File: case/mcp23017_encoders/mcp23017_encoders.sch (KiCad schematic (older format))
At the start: 7 parts

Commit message: revised schematic for pin numbering
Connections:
- net WiringPi_26 renamed WiringPi_27
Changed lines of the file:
@@
 $EndComp
 Text GLabel 6100 2700 2    60   Input ~ 0
-WiringPi_26
+WiringPi_27
 Text GLabel 6100 2600 2    60   Input ~ 0
 WiringPi_25

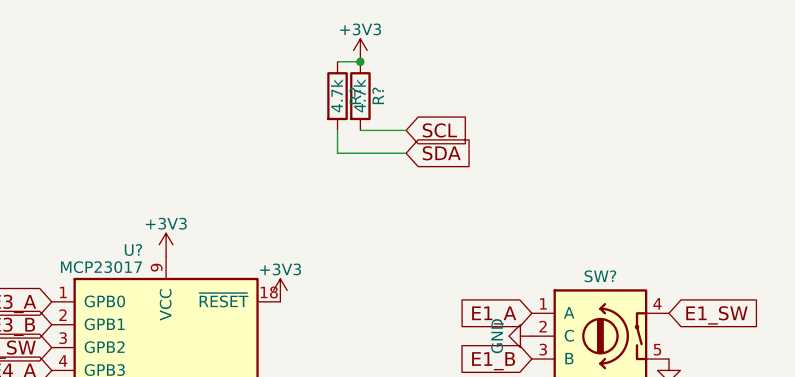
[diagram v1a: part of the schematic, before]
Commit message: removed pullups tt are not necessary on the raspberry pi
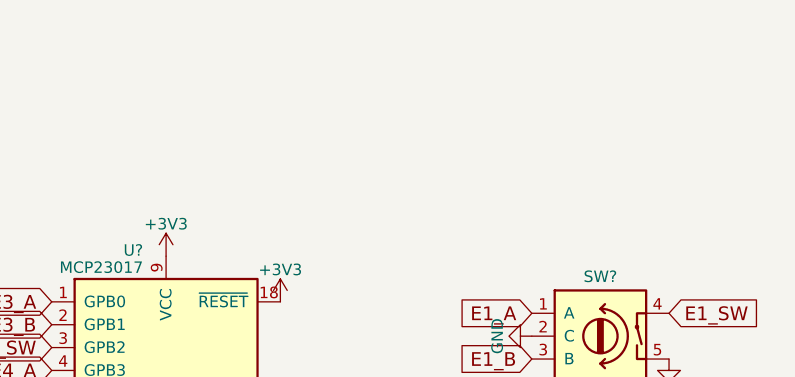
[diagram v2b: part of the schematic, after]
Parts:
- removed R? (x2): 4.7k, symbol R
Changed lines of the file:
@@
 	1    0    0    -1
 $EndComp
-Text GLabel 6650 1450 2    60   Input ~ 0
-SCL
-Text GLabel 6650 1550 2    60   Input ~ 0
-SDA
 Text GLabel 6100 3400 2    60   Input ~ 0
 SDA
 Text GLabel 6100 3300 2    60   Input ~ 0
 SCL
-$Comp
-L +3V3 #PWR?
-U 1 1 5936D9C5
-P 6450 1150
-F 0 "#PWR?" H 6450 1000 50  0001 C CNN
-F 1 "+3V3" H 6450 1290 50  0000 C CNN
-F 2 "" H 6450 1150 50  0001 C CNN
-F 3 "" H 6450 1150 50  0001 C CNN
-	1    6450 1150
-	1    0    0    -1
-$EndComp
-$Comp
-L R R?
-U 1 1 5936D9DF
-P 6450 1300
-F 0 "R?" V 6530 1300 50  0000 C CNN
-F 1 "4.7k" V 6450 1300 50  0000 C CNN
-F 2 "" V 6380 1300 50  0001 C CNN
-F 3 "" H 6450 1300 50  0001 C CNN
-	1    6450 1300
-	1    0    0    -1
-$EndComp
-$Comp
-L R R?
-U 1 1 5936DA26
-P 6350 1300
-F 0 "R?" V 6430 1300 50  0000 C CNN
-F 1 "4.7k" V 6350 1300 50  0000 C CNN
-F 2 "" V 6280 1300 50  0001 C CNN
-F 3 "" H 6350 1300 50  0001 C CNN
-	1    6350 1300
-	1    0    0    -1
-$EndComp
 $Comp
 L GND #PWR?
@@
 Wire Wire Line
 	6100 3600 6100 3800
-Connection ~ 6450 1150
-Wire Wire Line
-	6350 1550 6350 1450
-Wire Wire Line
-	6650 1550 6350 1550
-Wire Wire Line
-	6450 1450 6650 1450
-Wire Wire Line
-	6350 1150 6450 1150
 $Comp
 L GND #PWR?
